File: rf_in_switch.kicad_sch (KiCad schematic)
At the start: 9 parts, among them J13 Molex 73251-1153, J8 Molex 73251-1153, U31 QPC1022TR7, U32 QPC1022TR7

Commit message: Add an RF loopback test
Signed-off-by: Corey Minyard <corey@minyard.net>
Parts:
- removed R100, R99: 50, Resistor_SMD:R_0603_1608Metric_Pad0.98x0.95mm_HandSolder, symbol Device:R
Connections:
- net BOARD2_RF_BYPASS: now reaches U32.8 (RF2)
- net BOARD1_RF_BYPASS: now reaches U31.4 (RF1)

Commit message: Move to vertical SMA connectors
Required quite a bit of rework.

Signed-off-by: Corey Minyard <corey@minyard.net>
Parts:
- removed R97, R98: 10K, Resistor_SMD:R_0603_1608Metric_Pad0.98x0.95mm_HandSolder, symbol Device:R
- J13, J8: value Molex 73251-1153 -> Wirth 60312002114503; footprint Connector_Coaxial:SMA_Molex_73251-1153_EdgeMount_Horizontal -> Connector_Coaxial:SMA_Wurth_60312002114503_Vertical
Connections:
- net RF_SWITCH_EN: now reaches U31.6 (EN), U32.6 (EN)

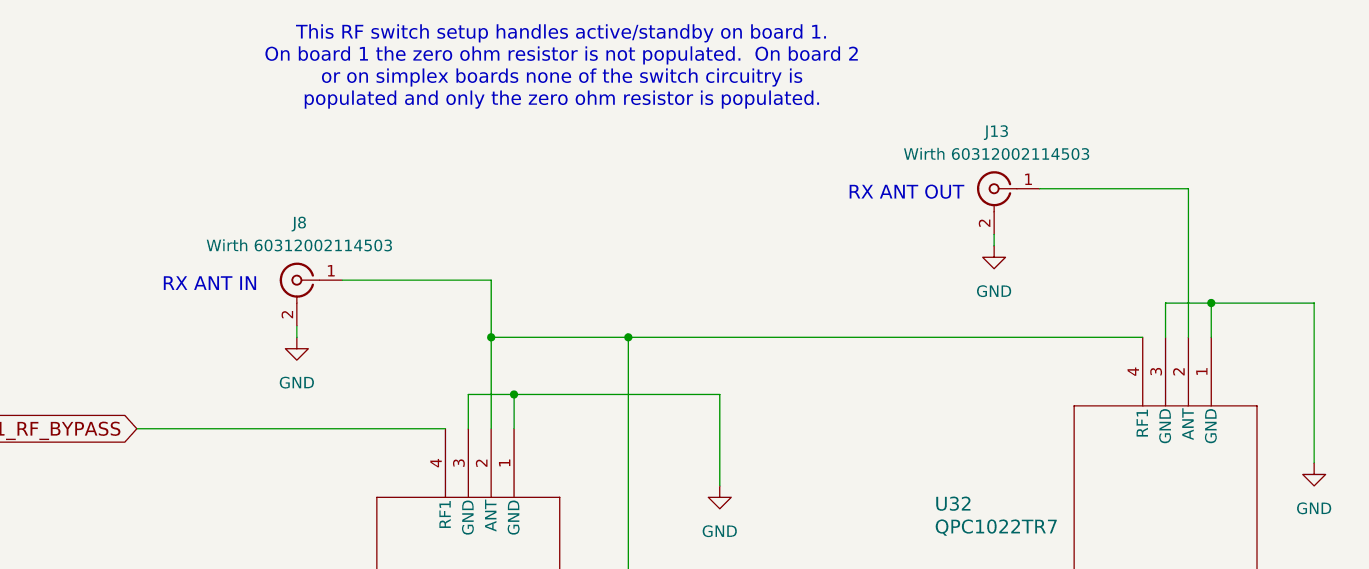
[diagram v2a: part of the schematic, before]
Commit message: Change RF connectors to U.FL
I'll solder a U.FL to SMA connector for testing.

Signed-off-by: Corey Minyard <corey@minyard.net>
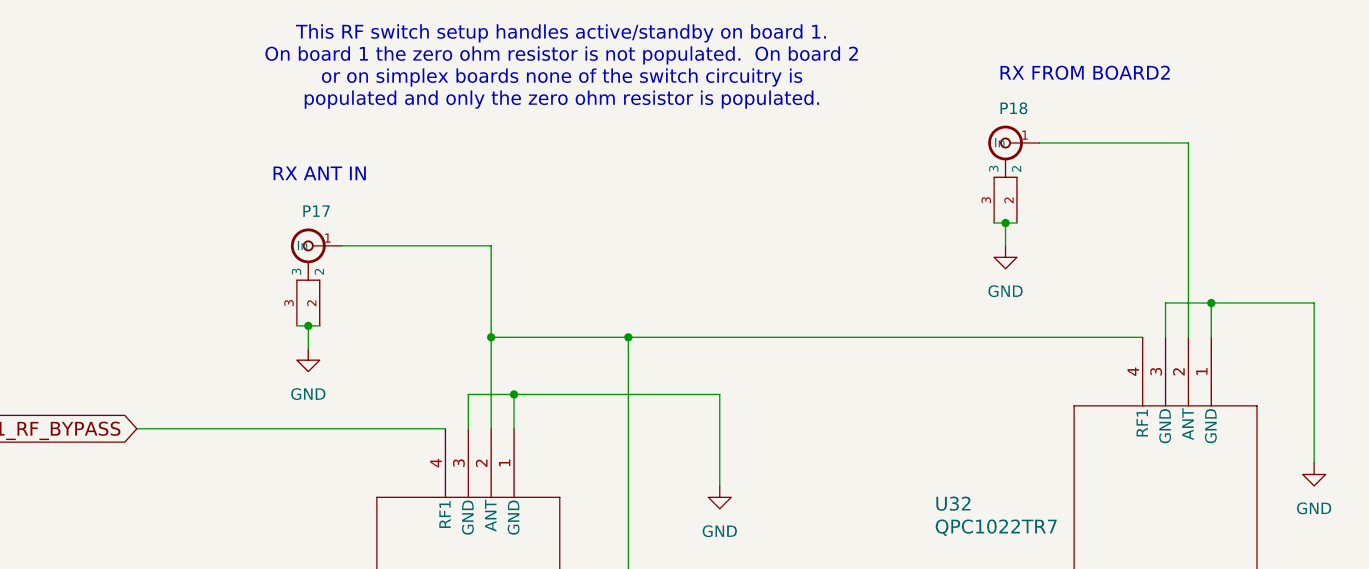
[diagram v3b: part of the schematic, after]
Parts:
- removed J13, J8: Wirth 60312002114503, Connector_Coaxial:SMA_Wurth_60312002114503_Vertical, symbol Connector:Conn_Coaxial
- added P17, P18: CONUFL001-SMD-T, PacSatDev_misc:CONN1_CONUFL_TEC, symbol PACSAT_DEV_misc:U_FL
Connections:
- net GND: now also P17.2, P17.3, P18.2, P18.3
- net at U32.2 (ANT): now also P18.1 (In)
- net at R96.1, U31.2 (ANT), U32.4 (RF1): now also P17.1 (In)
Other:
- note added: "RX FROM BOARD2"
- note removed: "RX ANT OUT"

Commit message: Add a current limiter for on-board +5V devices
Signed-off-by: Corey Minyard <corey@minyard.net>
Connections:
- net +5V renamed +5VAL
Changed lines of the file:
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@@
 			)
 		)
-		(property "Value" "+5V"
+		(property "Value" "+5VAL"
 			(at 83.82 113.03 0)
 			(effects

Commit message: Replace the output filter with a discrete one
The part chosen for the output filter didn't have very good ratings with
respect to being shaken and nothing on thermal cycles.  Also, it only
had 30dB of output filtering.  Replace with a discrete filter.

Signed-off-by: Corey Minyard <corey@minyard.net>
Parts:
- added L40: 470n, Inductor_SMD:L_0805_2012Metric_Pad1.05x1.20mm_HandSolder, symbol Device:L
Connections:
- net GND: now also L40.2
- net at P17.1 (In), R96.1, U31.2 (ANT)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: now also L40.1
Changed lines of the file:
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@@
+	)
+	(junction
+		(at 96.52 58.42)
+		(diameter 0)
+		(color 0 0 0 0)
 	)
 	(junction
@@
 	(wire
 		(pts
+			(xy 96.52 58.42) (xy 96.52 62.23)
+		)
+		(stroke
+			(width 0)
+			(type default)
+		)
+	)
+	(wire
+		(pts
 			(xy 99.06 120.65) (xy 139.7 120.65)
 		)
@@
 	(wire
 		(pts
-			(xy 90.17 58.42) (xy 106.68 58.42)
+			(xy 90.17 58.42) (xy 96.52 58.42)
 		)
 		(stroke
@@
 	(wire
 		(pts
+			(xy 96.52 58.42) (xy 106.68 58.42)
+		)
+		(stroke
+			(width 0)
+			(type default)
+		)
+	)
+	(wire
+		(pts
 			(xy 139.7 113.03) (xy 139.7 101.6)
+		)
+		(stroke
+			(width 0)
+			(type default)
+		)
+	)
+	(wire
+		(pts
+			(xy 96.52 69.85) (xy 96.52 72.39)
 		)
 		(stroke
@@
 	)
 	(symbol
+		(lib_id "power:GND")
+		(at 96.52 72.39 0)
+		(unit 1)
+		(exclude_from_sim no)
+		(in_bom yes)
+		(on_board yes)
+		(dnp no)
+		(property "Reference" "#PWR0293"
+			(at 96.52 78.74 0)
+			(effects
+				(font
+					(size 1.27 1.27)
+				)
+				(hide yes)
+			)
+		)
+		(property "Value" "GND"
+			(at 96.52 76.454 0)
+			(effects
+				(font
+					(size 1.27 1.27)
+				)
+			)
+		)
+		(property "Footprint" ""
+			(at 96.52 72.39 0)
+			(effects
+				(font
+					(size 1.27 1.27)
+				)
+				(hide yes)
+			)
+		)
+		(property "Datasheet" ""
+			(at 96.52 72.39 0)
+			(effects
+				(font
+					(size 1.27 1.27)
+				)
+				(hide yes)
+			)
+		)
+		(property "Description" ""
+			(at 96.52 72.39 0)
+			(effects
+				(font
+					(size 1.27 1.27)
+				)
+			)
+		)
+		(pin "1"
+		)
+		(instances
+			(project "PacSat_AFSK"
+				(path "/cc9f42d2-6985-41ac-acab-5ab7b01c5b38/4fa888af-703c-49ed-93bb-d56d2f02c470/64a91b23-a882-4658-bea9-c6c8274e2ac4"
+					(reference "#PWR0293")
+					(unit 1)
+				)
+			)
+		)
+	)
+	(symbol
 		(lib_id "PACSAT_DEV_misc:U_FL")
 		(at 163.83 46.99 0)
@@
 					(unit 1)
 				)
+			)
+		)
+	)
+	(symbol
+		(lib_id "Device:L")
+		(at 96.52 66.04 0)
+		(mirror y)
+		(unit 1)
+		(exclude_from_sim no)
+		(in_bom yes)
+		(on_board yes)
+		(dnp no)
+		(property "Reference" "L40"
+			(at 98.552 66.294 90)
+			(effects
+				(font
+					(size 1.27 1.27)
+				)
+			)
+		)
+		(property "Value" "470n"
+			(at 93.472 66.548 90)
+			(effects
+				(font
+					(size 1.27 1.27)
+				)
+			)
+		)
+		(property "Footprint" "Inductor_SMD:L_0805_2012Metric_Pad1.05x1.20mm_HandSolder"
+			(at 96.52 66.04 0)
+			(effects
+				(font
+					(size 1.27 1.27)
+				)
+				(hide yes)
+			)
+		)
+		(property "Datasheet" "~"
+			(at 96.52 66.04 0)
+			(effects
+				(font
+					(size 1.27 1.27)
+				)
+				(hide yes)
+			)
+		)
+		(property "Description" ""
+			(at 96.52 66.04 0)
+			(effects
+				(font
+					(size 1.27 1.27)
+				)
+			)
+		)
+		(pin "1"
+		)
+		(pin "2"
+		)
+		(instances
+			(project "PacSat_AFSK"
+				(path "/cc9f42d2-6985-41ac-acab-5ab7b01c5b38/4fa888af-703c-49ed-93bb-d56d2f02c470/64a91b23-a882-4658-bea9-c6c8274e2ac4"
+					(reference "L40")
+					(unit 1)
+				)

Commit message: Fix some notes
Signed-off-by: Corey Minyard <corey@minyard.net>
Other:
- note added: "Inductor to bleed off static build up on the antenna."
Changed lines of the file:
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@@
+		)
+	)
+	(text "Inductor to bleed off static build\nup on the antenna."
+		(exclude_from_sim no)
+		(at 115.824 55.118 0)
+		(effects
+			(font
+				(size 1.524 1.524)
+			)
 		)
 	)

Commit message: Lots of updates to ease manufacturing
Component changes, changes in the formatting of the values, etc.

Signed-off-by: Corey Minyard <corey@minyard.net>
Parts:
- L40: value 470n -> 470nH
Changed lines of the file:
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@@
 			)
 		)
-		(property "Value" "470n"
+		(property "Value" "470nH"
 			(at 93.472 66.548 90)
 			(effects

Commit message: Massive rework of filtering and inductors
Now that I know how inductors really work.

Signed-off-by: Corey Minyard <corey@minyard.net>
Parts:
- R96: now not fitted
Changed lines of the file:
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@@
 		(in_bom yes)
 		(on_board yes)
-		(dnp no)
+		(dnp yes)
 		(property "Reference" "R96"
 			(at 123.698 97.8916 0)
